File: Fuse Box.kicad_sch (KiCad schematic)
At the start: 17 parts, among them U1 DTM_2_Pin Male- #16, U2 DTM_2_Pin Female - #16, U3 DTM_2_Pin Male - #17, U4 DTM_2_Pin Female - #17, U5 DTM_12_Pin Male - #24

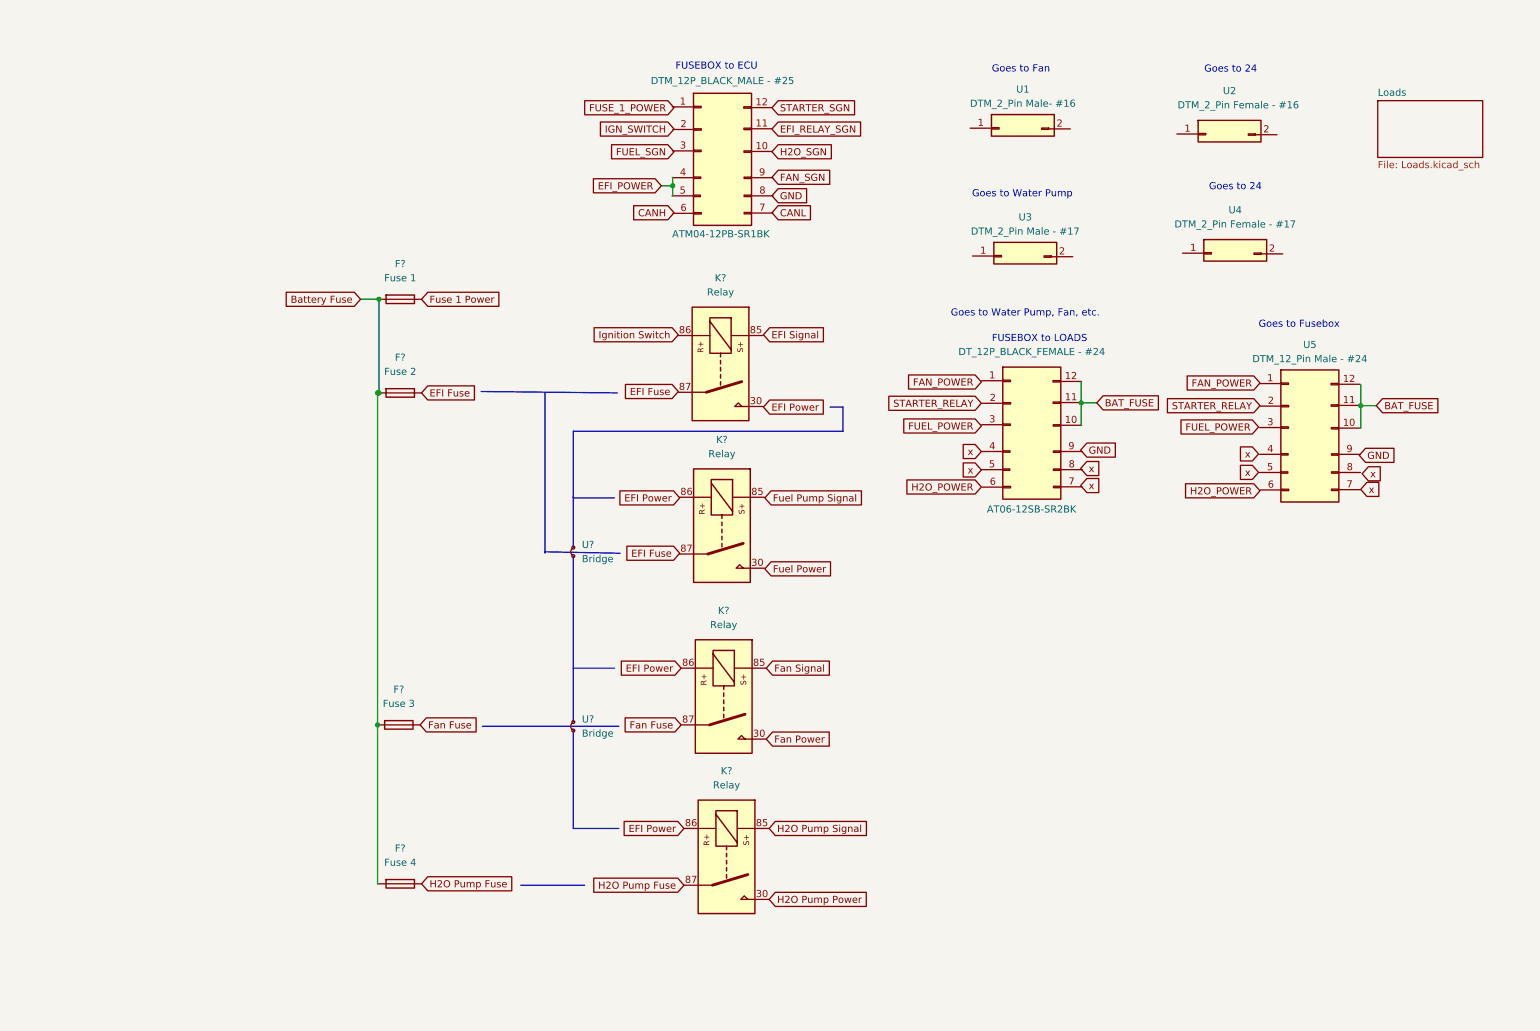
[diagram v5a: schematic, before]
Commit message: Updating Connectors
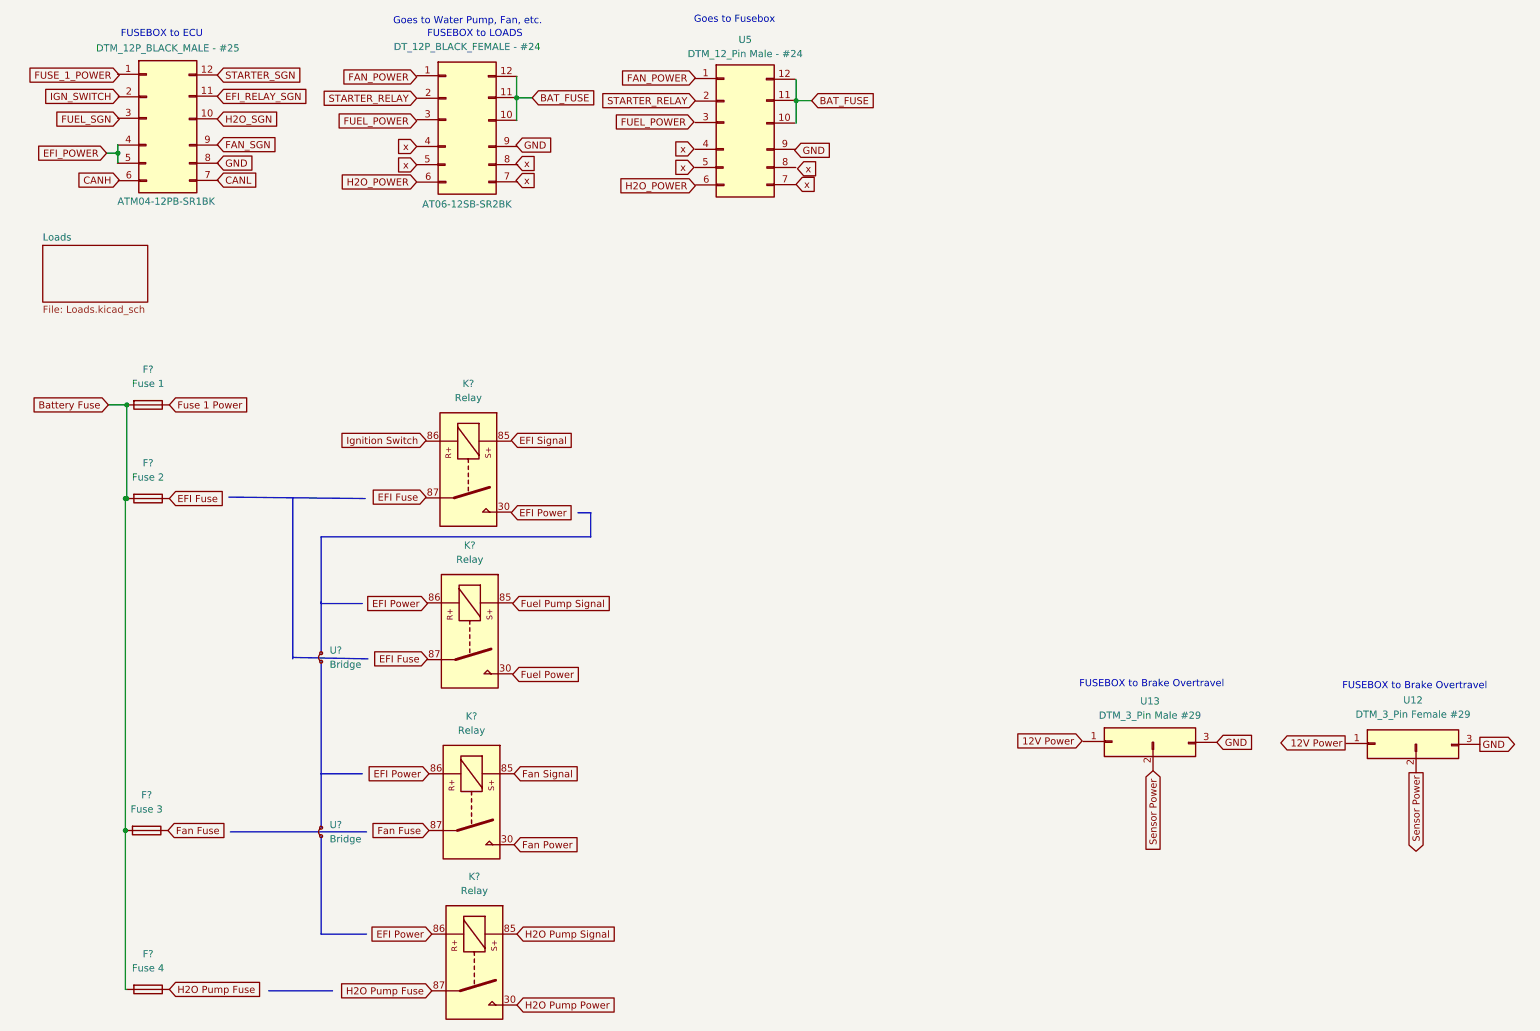
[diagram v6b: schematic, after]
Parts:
- removed U1: DTM_2_Pin Male- #16, symbol SCR23 Library:DTM_2_Pin
- removed U2: DTM_2_Pin Female - #16, symbol SCR23 Library:DTM_2_Pin
- removed U3: DTM_2_Pin Male - #17, symbol SCR23 Library:DTM_2_Pin
- removed U4: DTM_2_Pin Female - #17, symbol SCR23 Library:DTM_2_Pin
- added U12: DTM_3_Pin Female #29, symbol SCR23 Library:DTM_3_Pin
- added U13: DTM_3_Pin Male #29, symbol SCR23 Library:DTM_3_Pin
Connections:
- net GND: now also U12.3 (Pin_3), U13.3 (Pin_3)
- new net Sensor Power: U12.2 (Pin_2), U13.2 (Pin_2)
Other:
- note added: "FUSEBOX to Brake Overtravel"
- note removed: "Goes to 24"
- note removed: "Goes to Fan"
- note removed: "Goes to Water Pump"
- moved on the sheet: F?, K?, U5, U?
